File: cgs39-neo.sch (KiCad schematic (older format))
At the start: 65 parts, among them Q1 BC547, Q2 BC547, Q3 BC547, Q4 BC547, U1 TL074, U2 TL074

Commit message: idk
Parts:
- added R43, R44, R45, R46: 100K, symbol Device:R
- D1, D2, D3, D4: footprint (none) -> LED_THT:LED_D5.0mm
- InputA1, InputA2, InputB1, InputB2, InputC1, InputC2, InputD1, InputD2, OutputA1, OutputB1, OutputC1, OutputD1: footprint (none) -> Connector_Audio:Jack_6.35mm_Neutrik_NJ2FD-V_Vertical
- R1, R10, R11, R12, R13, R14, R15, R16, R17, R18, R19, R2, R20, R21, R22, R23, R24, R25, R26, R27, R28, R29, R3, R30, R31, R32, R33, R34, R35, R36, R37, R38, R39, R4, R40, R41, R42, R5, R6, R7, R8, R9: footprint (none) -> Resistor_THT:R_Axial_DIN0411_L9.9mm_D3.6mm_P15.24mm_Horizontal
- U1, U2: footprint (none) -> Package_DIP:DIP-14_W7.62mm
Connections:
- net GND: now also R43.1, R44.1, R45.1, R46.1
- net at OutputA1.T, R20.1: now also R44.2
- net at OutputD1.T, R41.1: now also R46.2
- net at OutputB1.T, R18.1: now also R43.2
- net at OutputC1.T, R39.1: now also R45.2

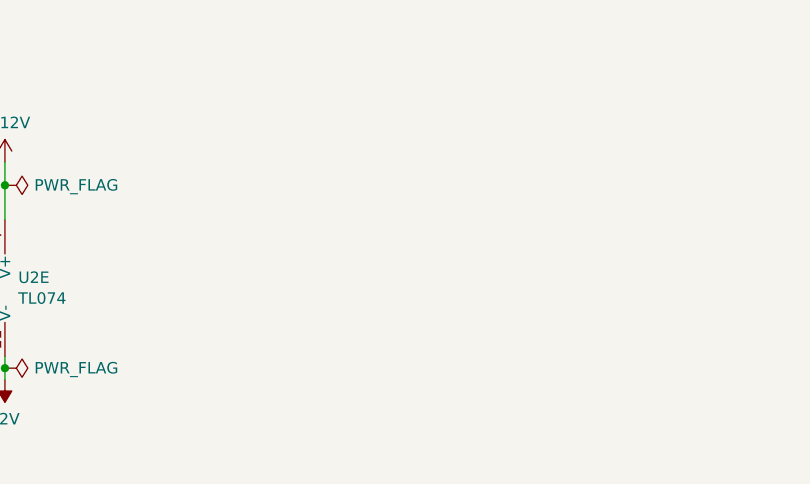
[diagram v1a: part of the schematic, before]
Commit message: add power & replace jacks
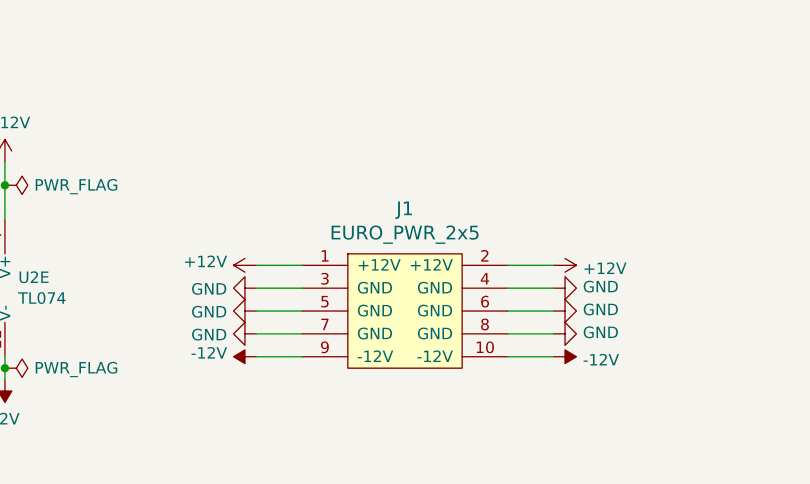
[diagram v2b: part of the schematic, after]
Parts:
- added J1: EURO_PWR_2x5, Connector_PinHeader_2.54mm:PinHeader_2x05_P2.54mm_Vertical, symbol eurocad:EURO_PWR_2x5
- InputA1, InputA2, InputB1, InputB2, InputC1, InputC2, InputD1, InputD2, OutputA1, OutputB1, OutputC1, OutputD1: footprint Connector_Audio:Jack_6.35mm_Neutrik_NJ2FD-V_Vertical -> cgs39-neo:SIMPLE-JACK-2PIN-THT
- R43, R44, R45, R46: footprint (none) -> Resistor_THT:R_Axial_DIN0411_L9.9mm_D3.6mm_P15.24mm_Horizontal
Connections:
- net +12V: now also J1.1 (+12V), J1.2 (+12V)
- net -12V: now also J1.10 (-12V), J1.9 (-12V)
- net GND: now also J1.3 (GND), J1.4 (GND), J1.5 (GND), J1.6 (GND), J1.7 (GND), J1.8 (GND)
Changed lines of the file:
@@
 F 0 "InputA1" H 1632 3775 50  0000 C CNN
 F 1 "AudioJack2" H 1632 3684 50  0000 C CNN
-F 2 "Connector_Audio:Jack_6.35mm_Neutrik_NJ2FD-V_Vertical" H 1600 3450 50  0001 C CNN
+F 2 "cgs39-neo:SIMPLE-JACK-2PIN-THT" H 1600 3450 50  0001 C CNN
 F 3 "~" H 1600 3450 50  0001 C CNN
 	1    1600 3450
@@
 F 0 "InputA2" H 1582 4675 50  0000 C CNN
 F 1 "AudioJack2" H 1582 4584 50  0000 C CNN
-F 2 "Connector_Audio:Jack_6.35mm_Neutrik_NJ2FD-V_Vertical" H 1550 4350 50  0001 C CNN
+F 2 "cgs39-neo:SIMPLE-JACK-2PIN-THT" H 1550 4350 50  0001 C CNN
 F 3 "~" H 1550 4350 50  0001 C CNN
 	1    1550 4350
@@
 F 0 "OutputA1" H 7182 3975 50  0000 C CNN
 F 1 "AudioJack2" H 7182 3884 50  0000 C CNN
-F 2 "Connector_Audio:Jack_6.35mm_Neutrik_NJ2FD-V_Vertical" H 7150 3650 50  0001 C CNN
+F 2 "cgs39-neo:SIMPLE-JACK-2PIN-THT" H 7150 3650 50  0001 C CNN
 F 3 "~" H 7150 3650 50  0001 C CNN
 	1    7150 3650
@@
 F 0 "InputB1" H 1582 6225 50  0000 C CNN
 F 1 "AudioJack2" H 1582 6134 50  0000 C CNN
-F 2 "Connector_Audio:Jack_6.35mm_Neutrik_NJ2FD-V_Vertical" H 1550 5900 50  0001 C CNN
+F 2 "cgs39-neo:SIMPLE-JACK-2PIN-THT" H 1550 5900 50  0001 C CNN
 F 3 "~" H 1550 5900 50  0001 C CNN
 	1    1550 5900
@@
 F 0 "InputB2" H 1532 7125 50  0000 C CNN
 F 1 "AudioJack2" H 1532 7034 50  0000 C CNN
-F 2 "Connector_Audio:Jack_6.35mm_Neutrik_NJ2FD-V_Vertical" H 1500 6800 50  0001 C CNN
+F 2 "cgs39-neo:SIMPLE-JACK-2PIN-THT" H 1500 6800 50  0001 C CNN
 F 3 "~" H 1500 6800 50  0001 C CNN
 	1    1500 6800
@@
 F 0 "OutputB1" H 7132 6425 50  0000 C CNN
 F 1 "AudioJack2" H 7132 6334 50  0000 C CNN
-F 2 "Connector_Audio:Jack_6.35mm_Neutrik_NJ2FD-V_Vertical" H 7100 6100 50  0001 C CNN
+F 2 "cgs39-neo:SIMPLE-JACK-2PIN-THT" H 7100 6100 50  0001 C CNN
 F 3 "~" H 7100 6100 50  0001 C CNN
 	1    7100 6100
@@
 F 0 "InputC1" H 9182 3875 50  0000 C CNN
 F 1 "AudioJack2" H 9182 3784 50  0000 C CNN
-F 2 "Connector_Audio:Jack_6.35mm_Neutrik_NJ2FD-V_Vertical" H 9150 3550 50  0001 C CNN
+F 2 "cgs39-neo:SIMPLE-JACK-2PIN-THT" H 9150 3550 50  0001 C CNN
 F 3 "~" H 9150 3550 50  0001 C CNN
 	1    9150 3550
@@
 F 0 "InputC2" H 9132 4775 50  0000 C CNN
 F 1 "AudioJack2" H 9132 4684 50  0000 C CNN
-F 2 "Connector_Audio:Jack_6.35mm_Neutrik_NJ2FD-V_Vertical" H 9100 4450 50  0001 C CNN
+F 2 "cgs39-neo:SIMPLE-JACK-2PIN-THT" H 9100 4450 50  0001 C CNN
 F 3 "~" H 9100 4450 50  0001 C CNN
 	1    9100 4450
@@
 F 0 "OutputC1" H 14732 4075 50  0000 C CNN
 F 1 "AudioJack2" H 14732 3984 50  0000 C CNN
-F 2 "Connector_Audio:Jack_6.35mm_Neutrik_NJ2FD-V_Vertical" H 14700 3750 50  0001 C CNN
+F 2 "cgs39-neo:SIMPLE-JACK-2PIN-THT" H 14700 3750 50  0001 C CNN
 F 3 "~" H 14700 3750 50  0001 C CNN
 	1    14700 3750
@@
 F 0 "InputD1" H 9182 6275 50  0000 C CNN
 F 1 "AudioJack2" H 9182 6184 50  0000 C CNN
-F 2 "Connector_Audio:Jack_6.35mm_Neutrik_NJ2FD-V_Vertical" H 9150 5950 50  0001 C CNN
+F 2 "cgs39-neo:SIMPLE-JACK-2PIN-THT" H 9150 5950 50  0001 C CNN
 F 3 "~" H 9150 5950 50  0001 C CNN
 	1    9150 5950
@@
 F 0 "InputD2" H 9132 7175 50  0000 C CNN
 F 1 "AudioJack2" H 9132 7084 50  0000 C CNN
-F 2 "Connector_Audio:Jack_6.35mm_Neutrik_NJ2FD-V_Vertical" H 9100 6850 50  0001 C CNN
+F 2 "cgs39-neo:SIMPLE-JACK-2PIN-THT" H 9100 6850 50  0001 C CNN
 F 3 "~" H 9100 6850 50  0001 C CNN
 	1    9100 6850
@@
 F 0 "OutputD1" H 14732 6475 50  0000 C CNN
 F 1 "AudioJack2" H 14732 6384 50  0000 C CNN
-F 2 "Connector_Audio:Jack_6.35mm_Neutrik_NJ2FD-V_Vertical" H 14700 6150 50  0001 C CNN
+F 2 "cgs39-neo:SIMPLE-JACK-2PIN-THT" H 14700 6150 50  0001 C CNN
 F 3 "~" H 14700 6150 50  0001 C CNN
 	1    14700 6150
@@
 F 0 "R45" H 14570 3496 50  0000 L CNN
 F 1 "100K" H 14570 3405 50  0000 L CNN
-F 2 "" V 14430 3450 50  0001 C CNN
+F 2 "Resistor_THT:R_Axial_DIN0411_L9.9mm_D3.6mm_P15.24mm_Horizontal" V 14430 3450 50  0001 C CNN
 F 3 "~" H 14500 3450 50  0001 C CNN
 	1    14500 3450
@@
 F 0 "R46" H 14570 5896 50  0000 L CNN
 F 1 "100K" H 14570 5805 50  0000 L CNN
-F 2 "" V 14430 5850 50  0001 C CNN
+F 2 "Resistor_THT:R_Axial_DIN0411_L9.9mm_D3.6mm_P15.24mm_Horizontal" V 14430 5850 50  0001 C CNN
 F 3 "~" H 14500 5850 50  0001 C CNN
 	1    14500 5850
@@
 F 0 "R43" H 6970 5846 50  0000 L CNN
 F 1 "100K" H 6970 5755 50  0000 L CNN
-F 2 "" V 6830 5800 50  0001 C CNN
+F 2 "Resistor_THT:R_Axial_DIN0411_L9.9mm_D3.6mm_P15.24mm_Horizontal" V 6830 5800 50  0001 C CNN
 F 3 "~" H 6900 5800 50  0001 C CNN
 	1    6900 5800
@@
 F 0 "R44" H 7020 3396 50  0000 L CNN
 F 1 "100K" H 7020 3305 50  0000 L CNN
-F 2 "" V 6880 3350 50  0001 C CNN
+F 2 "Resistor_THT:R_Axial_DIN0411_L9.9mm_D3.6mm_P15.24mm_Horizontal" V 6880 3350 50  0001 C CNN
 F 3 "~" H 6950 3350 50  0001 C CNN
 	1    6950 3350
@@
 Wire Wire Line
 	6950 3500 6950 3650
+$Comp
+L eurocad:EURO_PWR_2x5 J1
+U 1 1 5FBBEE4E
+P 7000 9150
+F 0 "J1" H 7000 9597 60  0000 C CNN
+F 1 "EURO_PWR_2x5" H 7000 9491 60  0000 C CNN
+F 2 "Connector_PinHeader_2.54mm:PinHeader_2x05_P2.54mm_Vertical" H 7000 9150 60  0001 C CNN
+F 3 "" H 7000 9150 60  0000 C CNN
+	1    7000 9150
+	1    0    0    -1
+$EndComp
+$Comp
+L power:+12V #PWR06
+U 1 1 5FBD83D4
+P 7650 8950
+F 0 "#PWR06" H 7650 8800 50  0001 C CNN
+F 1 "+12V" V 7665 9078 50  0000 L CNN
+F 2 "" H 7650 8950 50  0001 C CNN
+F 3 "" H 7650 8950 50  0001 C CNN
+	1    7650 8950
+	0    1    1    0
+$EndComp
+$Comp
+L power:+12V #PWR01
+U 1 1 5FBE17CE
+P 6350 8950
+F 0 "#PWR01" H 6350 8800 50  0001 C CNN
+F 1 "+12V" V 6365 9078 50  0000 L CNN
+F 2 "" H 6350 8950 50  0001 C CNN
+F 3 "" H 6350 8950 50  0001 C CNN
+	1    6350 8950
+	0    -1   -1   0
+$EndComp
+$Comp
+L power:-12V #PWR010
+U 1 1 5FBF67EB
+P 7650 9350
+F 0 "#PWR010" H 7650 9450 50  0001 C CNN
+F 1 "-12V" V 7665 9478 50  0000 L CNN
+F 2 "" H 7650 9350 50  0001 C CNN
+F 3 "" H 7650 9350 50  0001 C CNN
+	1    7650 9350
+	0    1    1    0
+$EndComp
+$Comp
+L power:-12V #PWR05
+U 1 1 5FBFAA22
+P 6350 9350
+F 0 "#PWR05" H 6350 9450 50  0001 C CNN
+F 1 "-12V" V 6365 9478 50  0000 L CNN
+F 2 "" H 6350 9350 50  0001 C CNN
+F 3 "" H 6350 9350 50  0001 C CNN
+	1    6350 9350
+	0    -1   -1   0
+$EndComp
+$Comp
+L power:GND #PWR07
+U 1 1 5FC04D30
+P 7650 9050
+F 0 "#PWR07" H 7650 8800 50  0001 C CNN
+F 1 "GND" V 7655 8922 50  0000 R CNN
+F 2 "" H 7650 9050 50  0001 C CNN
+F 3 "" H 7650 9050 50  0001 C CNN
+	1    7650 9050
+	0    -1   -1   0
+$EndComp
+$Comp
+L power:GND #PWR08
+U 1 1 5FC063FC
+P 7650 9150
+F 0 "#PWR08" H 7650 8900 50  0001 C CNN
+F 1 "GND" V 7655 9022 50  0000 R CNN
+F 2 "" H 7650 9150 50  0001 C CNN
+F 3 "" H 7650 9150 50  0001 C CNN
+	1    7650 9150
+	0    -1   -1   0
+$EndComp
+$Comp
+L power:GND #PWR09
+U 1 1 5FC0685F
+P 7650 9250
+F 0 "#PWR09" H 7650 9000 50  0001 C CNN
+F 1 "GND" V 7655 9122 50  0000 R CNN
+F 2 "" H 7650 9250 50  0001 C CNN
+F 3 "" H 7650 9250 50  0001 C CNN
+	1    7650 9250
+	0    -1   -1   0
+$EndComp
+$Comp
+L power:GND #PWR02
+U 1 1 5FC06C7C
+P 6350 9050
+F 0 "#PWR02" H 6350 8800 50  0001 C CNN
+F 1 "GND" V 6355 8922 50  0000 R CNN
+F 2 "" H 6350 9050 50  0001 C CNN
+F 3 "" H 6350 9050 50  0001 C CNN
+	1    6350 9050
+	0    1    1    0
+$EndComp
+$Comp
+L power:GND #PWR03
+U 1 1 5FC07599
+P 6350 9150
+F 0 "#PWR03" H 6350 8900 50  0001 C CNN
+F 1 "GND" V 6355 9022 50  0000 R CNN
+F 2 "" H 6350 9150 50  0001 C CNN
+F 3 "" H 6350 9150 50  0001 C CNN
+	1    6350 9150
+	0    1    1    0
+$EndComp
+$Comp
+L power:GND #PWR04
+U 1 1 5FC07C09
+P 6350 9250
+F 0 "#PWR04" H 6350 9000 50  0001 C CNN
+F 1 "GND" V 6355 9122 50  0000 R CNN
+F 2 "" H 6350 9250 50  0001 C CNN
+F 3 "" H 6350 9250 50  0001 C CNN
+	1    6350 9250
+	0    1    1    0
+$EndComp
+Wire Wire Line
+	6350 8950 6550 8950
+Wire Wire Line
+	6550 9050 6350 9050
+Wire Wire Line
+	6350 9150 6550 9150
+Wire Wire Line
+	6350 9250 6550 9250
+Wire Wire Line
+	6350 9350 6550 9350
+Wire Wire Line
+	7450 8950 7650 8950
+Wire Wire Line
+	7650 9050 7450 9050
+Wire Wire Line
+	7450 9150 7650 9150
+Wire Wire Line
+	7650 9250 7450 9250
+Wire Wire Line
+	7450 9350 7650 9350
 $EndSCHEMATC

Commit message: i hate this
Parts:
- R1, R10, R11, R12, R13, R14, R15, R16, R17, R18, R19, R2, R20, R21, R22, R23, R24, R25, R26, R27, R28, R29, R3, R30, R31, R32, R33, R34, R35, R36, R37, R38, R39, R4, R40, R41, R42, R43, R44, R45, R46, R5, R6, R7, R8, R9: footprint Resistor_THT:R_Axial_DIN0411_L9.9mm_D3.6mm_P15.24mm_Horizontal -> Resistor_THT:R_Axial_DIN0204_L3.6mm_D1.6mm_P5.08mm_Horizontal
